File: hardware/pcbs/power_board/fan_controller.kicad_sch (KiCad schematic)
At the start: 10 parts, among them J10 Molex 22-23-2031, J11 Molex 22-23-2031, J12 Molex 22-23-2031, J9 Molex 22-23-2031, U10 EMC2305, U11 4069

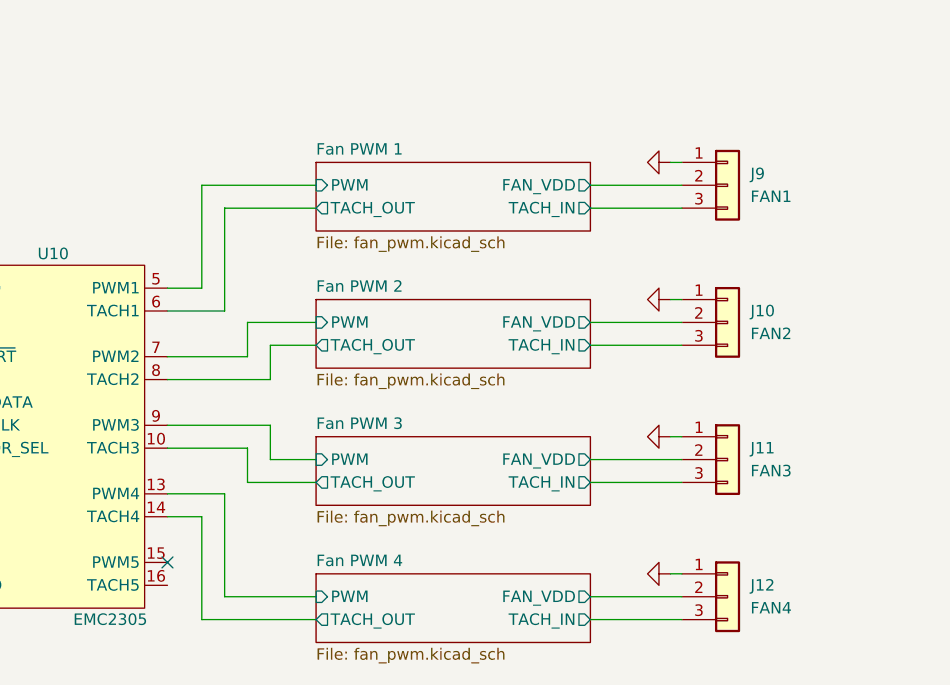
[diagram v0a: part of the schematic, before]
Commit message: power_board: final-ish shape
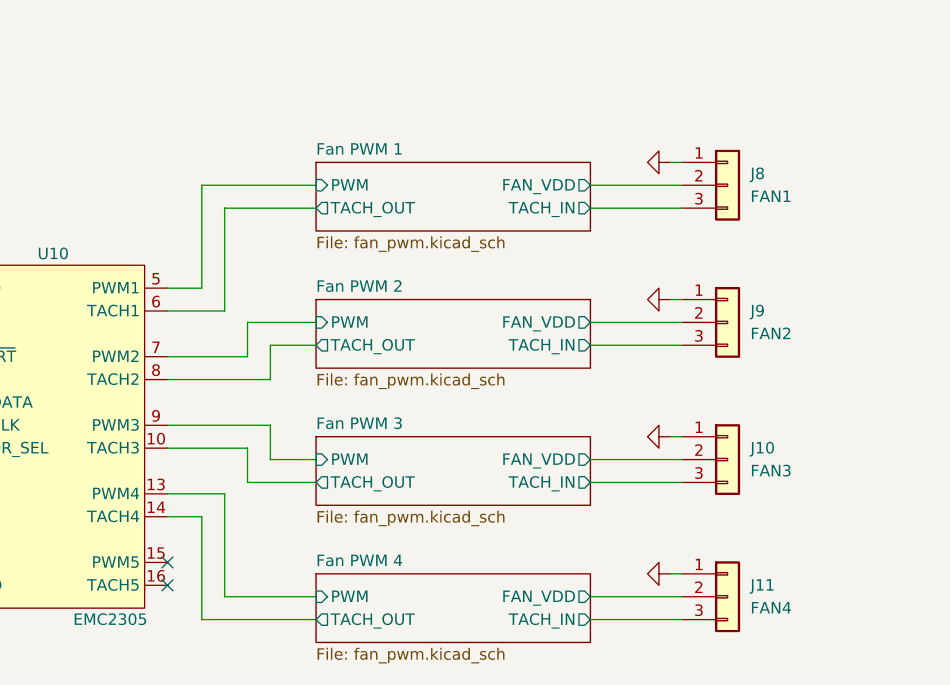
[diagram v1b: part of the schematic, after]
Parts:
- renumbered J11 to J10, J12 to J11, J9 to J8, J10 to J9
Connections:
- no-connect marks 3 -> 4
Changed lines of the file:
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@@
+	)
+	(no_connect
+		(at 137.16 129.54)
 	)
 	(no_connect
@@
 		(on_board yes)
 		(dnp no)
-		(property "Reference" "J9"
+		(property "Reference" "J8"
 			(at 201.93 83.8199 0)
 			(effects
@@
 			(project "power_board"
 				(path "/4b166175-80a4-48c6-994d-6e62a6160b87/f4395b92-97ec-456a-b4c2-238b75f494a2"
-					(reference "J9")
+					(reference "J8")
 					(unit 1)
 				)
@@
 		(on_board yes)
 		(dnp no)
-		(property "Reference" "J11"
+		(property "Reference" "J10"
 			(at 201.93 114.2999 0)
 			(effects
@@
 			(project "power_board"
 				(path "/4b166175-80a4-48c6-994d-6e62a6160b87/f4395b92-97ec-456a-b4c2-238b75f494a2"
-					(reference "J11")
+					(reference "J10")
 					(unit 1)
 				)
@@
 		(on_board yes)
 		(dnp no)
-		(property "Reference" "J10"
+		(property "Reference" "J9"
 			(at 201.93 99.0599 0)
 			(effects
@@
 			(project "power_board"
 				(path "/4b166175-80a4-48c6-994d-6e62a6160b87/f4395b92-97ec-456a-b4c2-238b75f494a2"
-					(reference "J10")
+					(reference "J9")
 					(unit 1)
 				)
@@
 		(on_board yes)
 		(dnp no)
-		(property "Reference" "J12"
+		(property "Reference" "J11"
 			(at 201.93 129.5399 0)
 			(effects
@@
 			(project "power_board"
 				(path "/4b166175-80a4-48c6-994d-6e62a6160b87/f4395b92-97ec-456a-b4c2-238b75f494a2"
-					(reference "J12")
+					(reference "J11")
 					(unit 1)
 				)

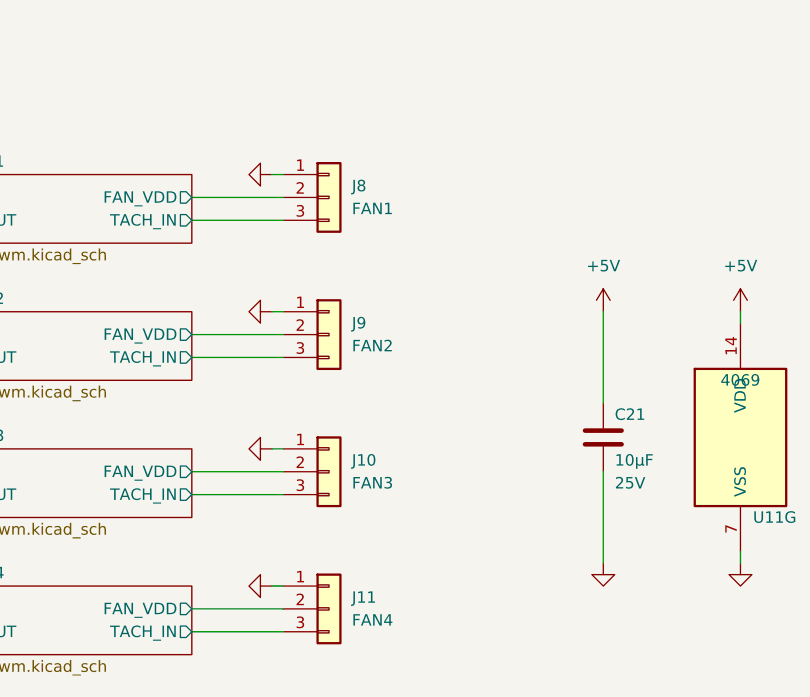
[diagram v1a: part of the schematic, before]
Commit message: power_board: use purpose labels on connectors
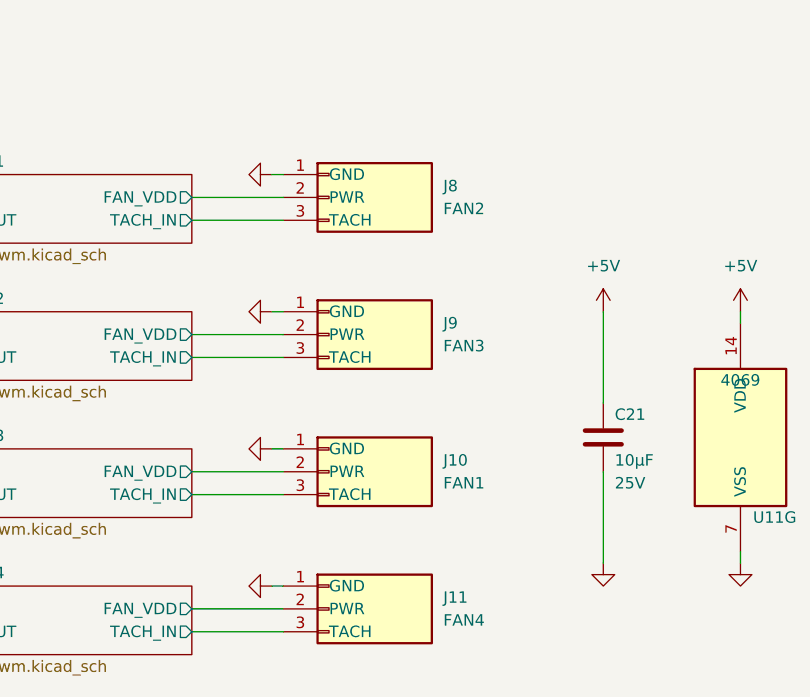
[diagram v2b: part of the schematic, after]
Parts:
- removed J10, J11, J8, J9: Molex 22-23-2031, Connector_MTA-100:mta100_01x3_P2.54_647050-3, symbol Connector_Generic:Conn_01x03
- added J10, J11, J8, J9: Header_01x03, Connector_MTA-100:mta100_01x3_P2.54_647050-3, symbol conn:Conn_01x03
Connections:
- net Fan PWM 1/FAN_VDD: now also J8.2 (Pin_2)
- net Fan PWM 1/TACH_IN: now also J8.3 (Pin_3)
- net Fan PWM 2/FAN_VDD: now also J9.2 (Pin_2)
- net Fan PWM 2/TACH_IN: now also J9.3 (Pin_3)
- net Fan PWM 3/FAN_VDD: now also J10.2 (Pin_2)
- net Fan PWM 3/TACH_IN: now also J10.3 (Pin_3)
- net Fan PWM 4/FAN_VDD: now also J11.2 (Pin_2)
- net Fan PWM 4/TACH_IN: now also J11.3 (Pin_3)
- net GND: now also J10.1 (Pin_1), J11.1 (Pin_1), J8.1 (Pin_1), J9.1 (Pin_1)

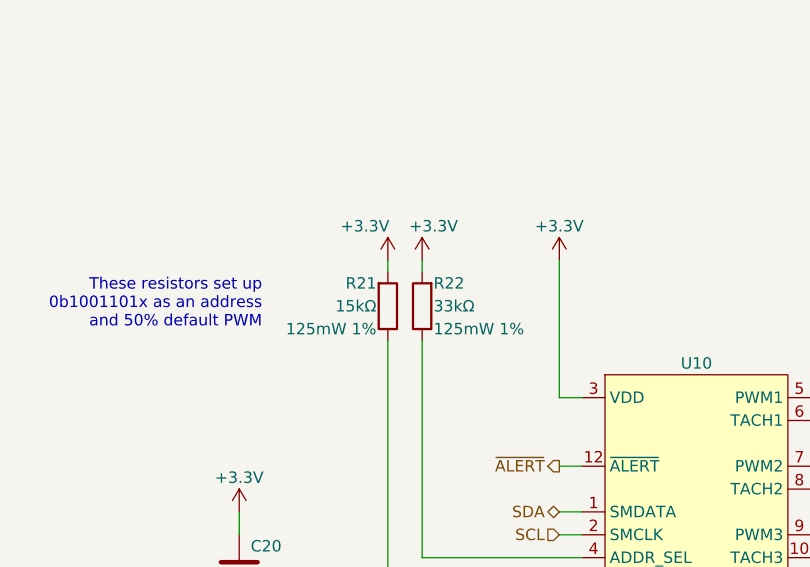
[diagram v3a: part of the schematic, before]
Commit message: power_board: use USB3-A passthrough connector and fix chg EN
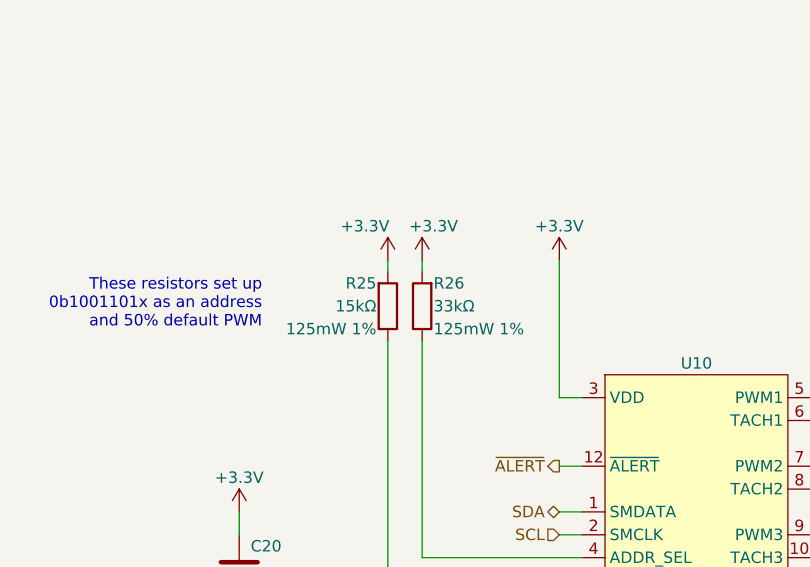
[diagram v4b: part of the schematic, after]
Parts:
- renumbered R21 to R25, R22 to R26
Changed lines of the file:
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@@
 		(on_board yes)
 		(dnp no)
-		(property "Reference" "R22"
+		(property "Reference" "R26"
 			(at 95.25 83.82 0)
 			(effects
@@
 			(project "power_board"
 				(path "/4b166175-80a4-48c6-994d-6e62a6160b87/f4395b92-97ec-456a-b4c2-238b75f494a2"
-					(reference "R22")
+					(reference "R26")
 					(unit 1)
 				)
@@
 		(on_board yes)
 		(dnp no)
-		(property "Reference" "R21"
+		(property "Reference" "R25"
 			(at 88.9 83.82 0)
 			(effects
@@
 			(project "power_board"
 				(path "/4b166175-80a4-48c6-994d-6e62a6160b87/f4395b92-97ec-456a-b4c2-238b75f494a2"
-					(reference "R21")
-					(unit 1)
-				)
+					(reference "R25")
+					(unit 1)
+				)

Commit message: power_board: add protection resistor to overload signal
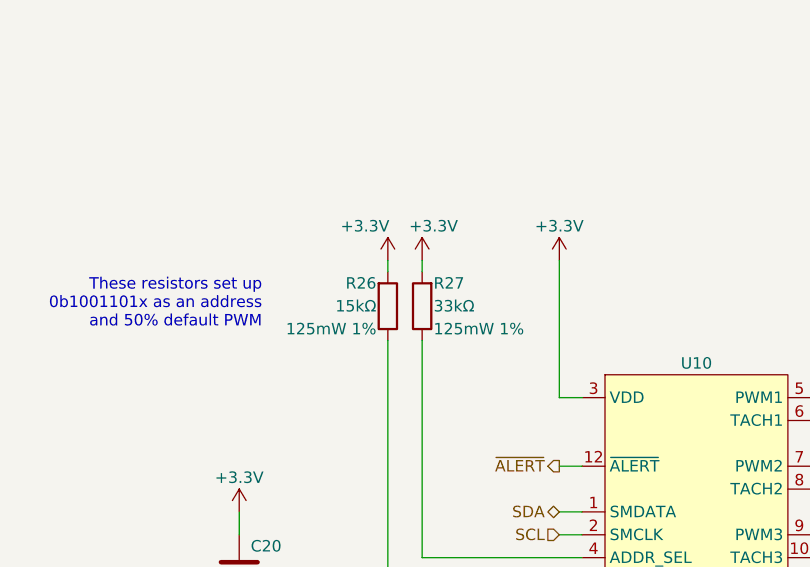
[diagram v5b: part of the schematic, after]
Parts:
- renumbered R25 to R26, R26 to R27
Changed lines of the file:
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@@
 		(on_board yes)
 		(dnp no)
-		(property "Reference" "R26"
+		(property "Reference" "R27"
 			(at 95.25 83.82 0)
 			(effects
@@
 			(project "power_board"
 				(path "/4b166175-80a4-48c6-994d-6e62a6160b87/f4395b92-97ec-456a-b4c2-238b75f494a2"
-					(reference "R26")
+					(reference "R27")
 					(unit 1)
 				)
@@
 		(on_board yes)
 		(dnp no)
-		(property "Reference" "R25"
+		(property "Reference" "R26"
 			(at 88.9 83.82 0)
 			(effects
@@
 			(project "power_board"
 				(path "/4b166175-80a4-48c6-994d-6e62a6160b87/f4395b92-97ec-456a-b4c2-238b75f494a2"
-					(reference "R25")
-					(unit 1)
-				)
+					(reference "R26")
+					(unit 1)
+				)

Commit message: boards: update wrong shop links
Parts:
- C20: Shop https://store.comet.bg/Catalogue/Product/16789/ -> https://store.comet.bg/Catalogue/Product/6645/
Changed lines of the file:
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@@
 			)
 		)
-		(property "Shop" "https://store.comet.bg/Catalogue/Product/16789/"
+		(property "Shop" "https://store.comet.bg/Catalogue/Product/6645/"
 			(at 73.66 115.57 0)
 			(effects

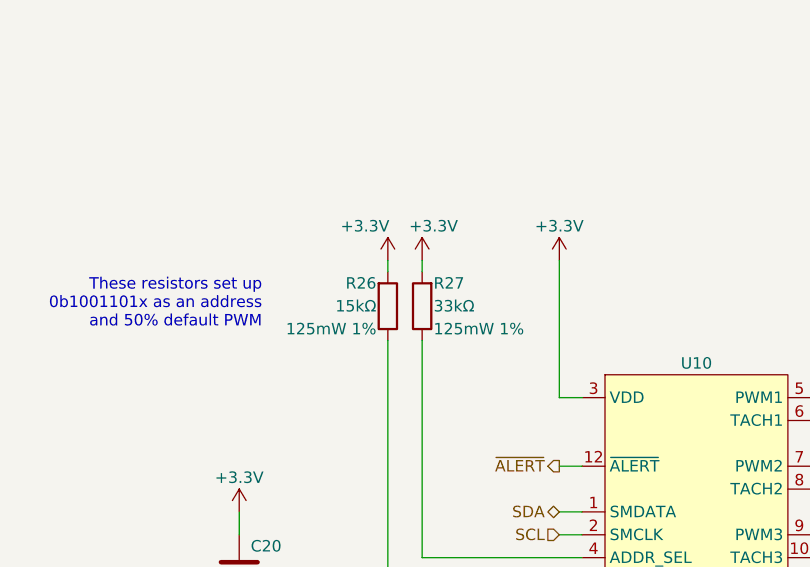
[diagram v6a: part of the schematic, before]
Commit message: power_board: proper enable circuit for meanwell power modules
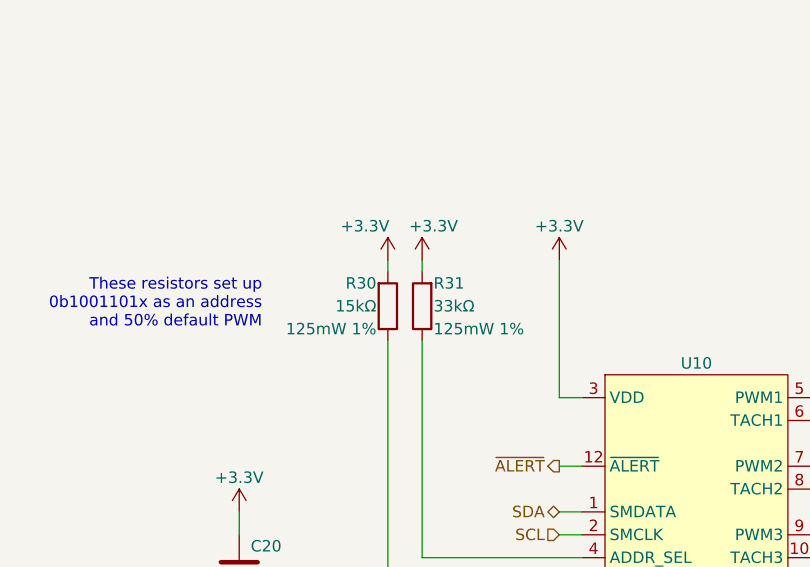
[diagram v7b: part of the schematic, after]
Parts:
- renumbered R26 to R30, R27 to R31
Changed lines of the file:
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@@
 		(on_board yes)
 		(dnp no)
-		(property "Reference" "R27"
+		(property "Reference" "R31"
 			(at 95.25 83.82 0)
 			(effects
@@
 			(project "power_board"
 				(path "/4b166175-80a4-48c6-994d-6e62a6160b87/f4395b92-97ec-456a-b4c2-238b75f494a2"
-					(reference "R27")
+					(reference "R31")
 					(unit 1)
 				)
@@
 		(on_board yes)
 		(dnp no)
-		(property "Reference" "R26"
+		(property "Reference" "R30"
 			(at 88.9 83.82 0)
 			(effects
@@
 			(project "power_board"
 				(path "/4b166175-80a4-48c6-994d-6e62a6160b87/f4395b92-97ec-456a-b4c2-238b75f494a2"
-					(reference "R26")
-					(unit 1)
-				)
+					(reference "R30")
+					(unit 1)
+				)

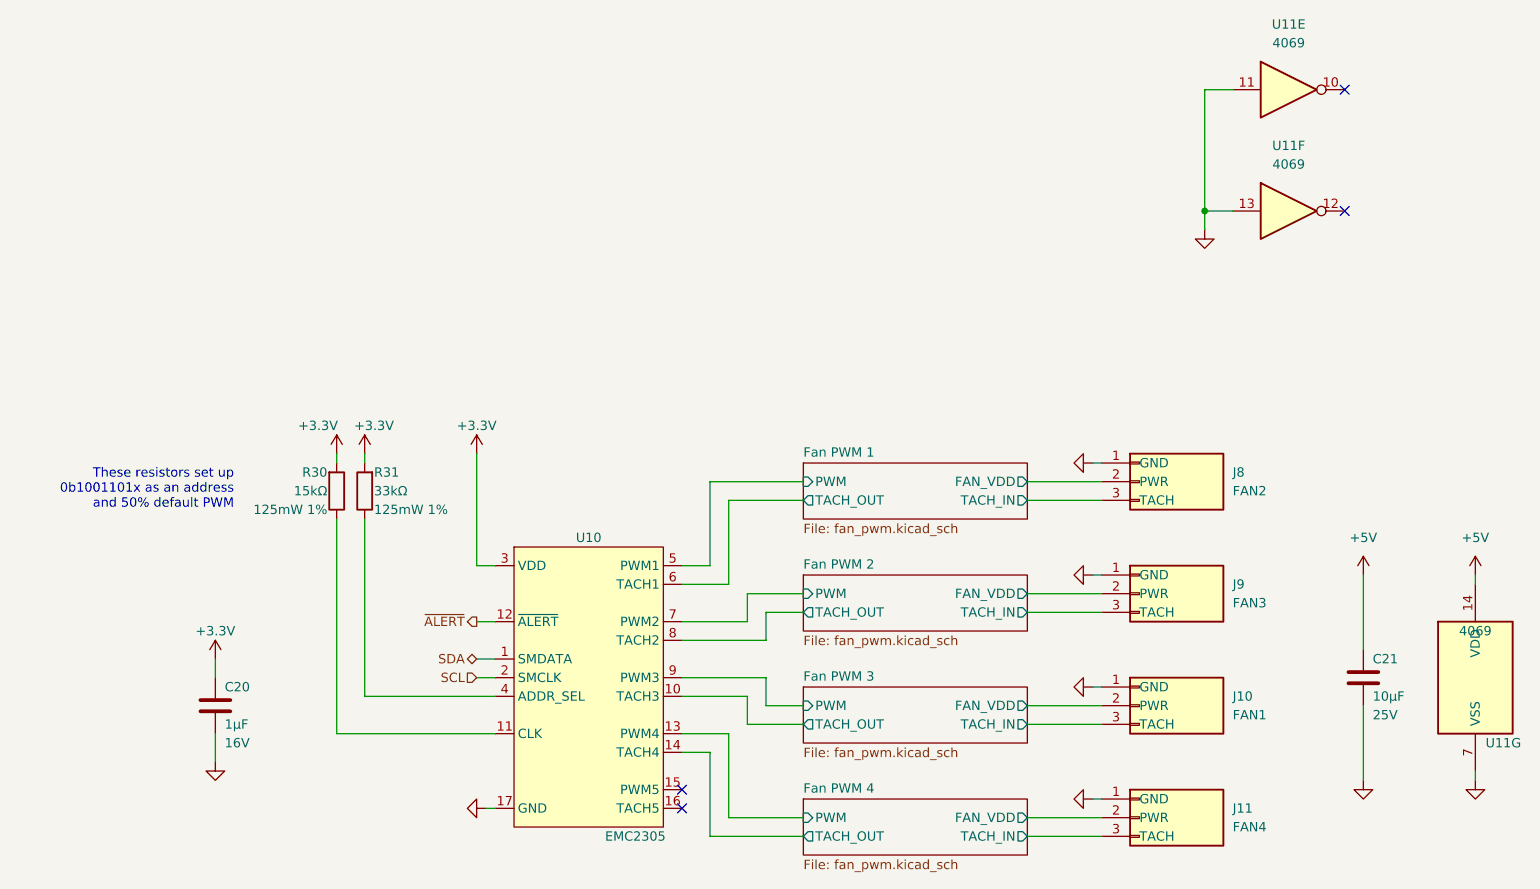
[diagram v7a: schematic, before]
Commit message: power_board: axe one fan output to make space for caps
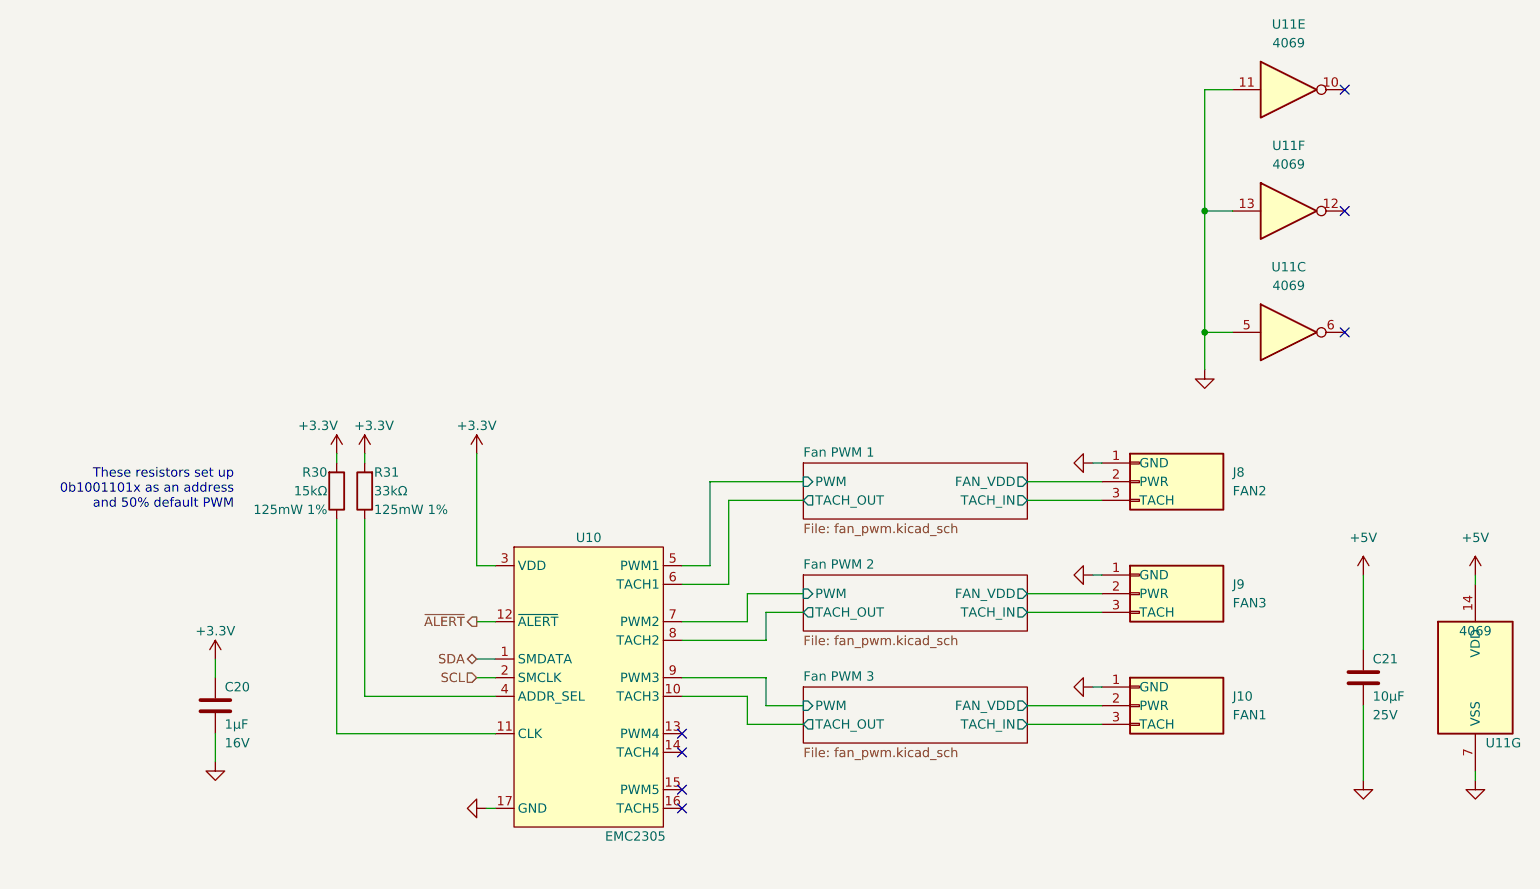
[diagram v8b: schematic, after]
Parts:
- removed J11: Header_01x03, Connector_MTA-100:mta100_01x3_P2.54_647050-3, symbol conn:Conn_01x03
- added unit 3 of U11
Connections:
- net GND: now also U11.5
- net Fan PWM 4/PWM: no longer names the net of U10.13 (PWM4)
- net Fan PWM 4/TACH_OUT: no longer names the net of U10.14 (TACH4)
- no-connect marks 4 -> 7
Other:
- removed sheet Fan PWM 4
